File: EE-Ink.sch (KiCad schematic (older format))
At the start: 24 parts, among them U1 ED060SC4

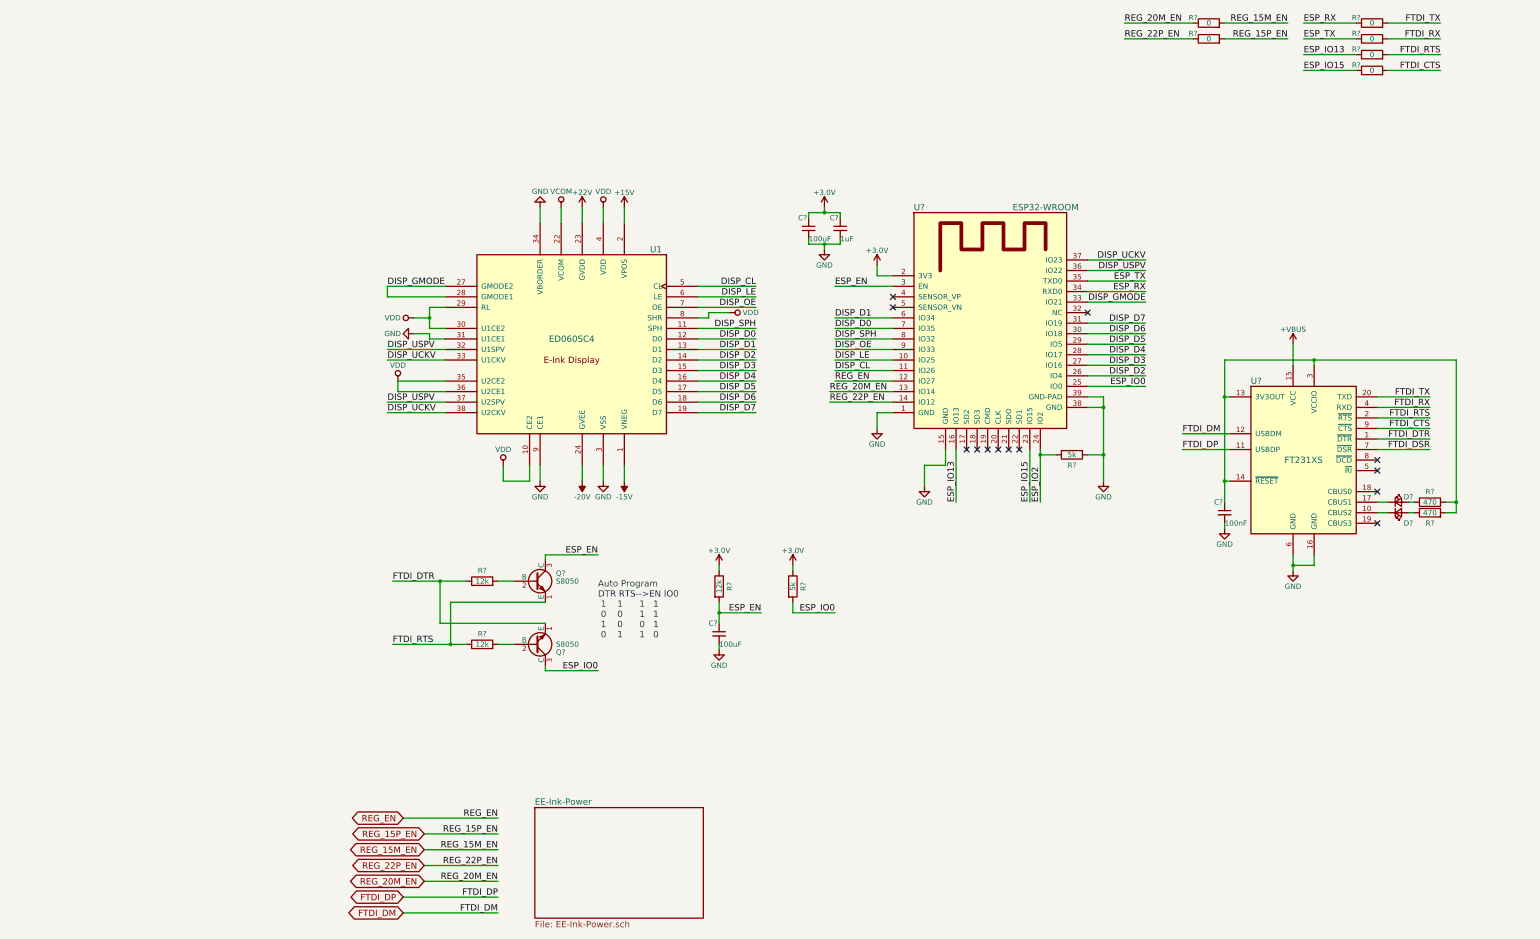
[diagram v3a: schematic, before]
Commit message: Switched out the regulator for a 500ma one.  Cleaned up a few things.
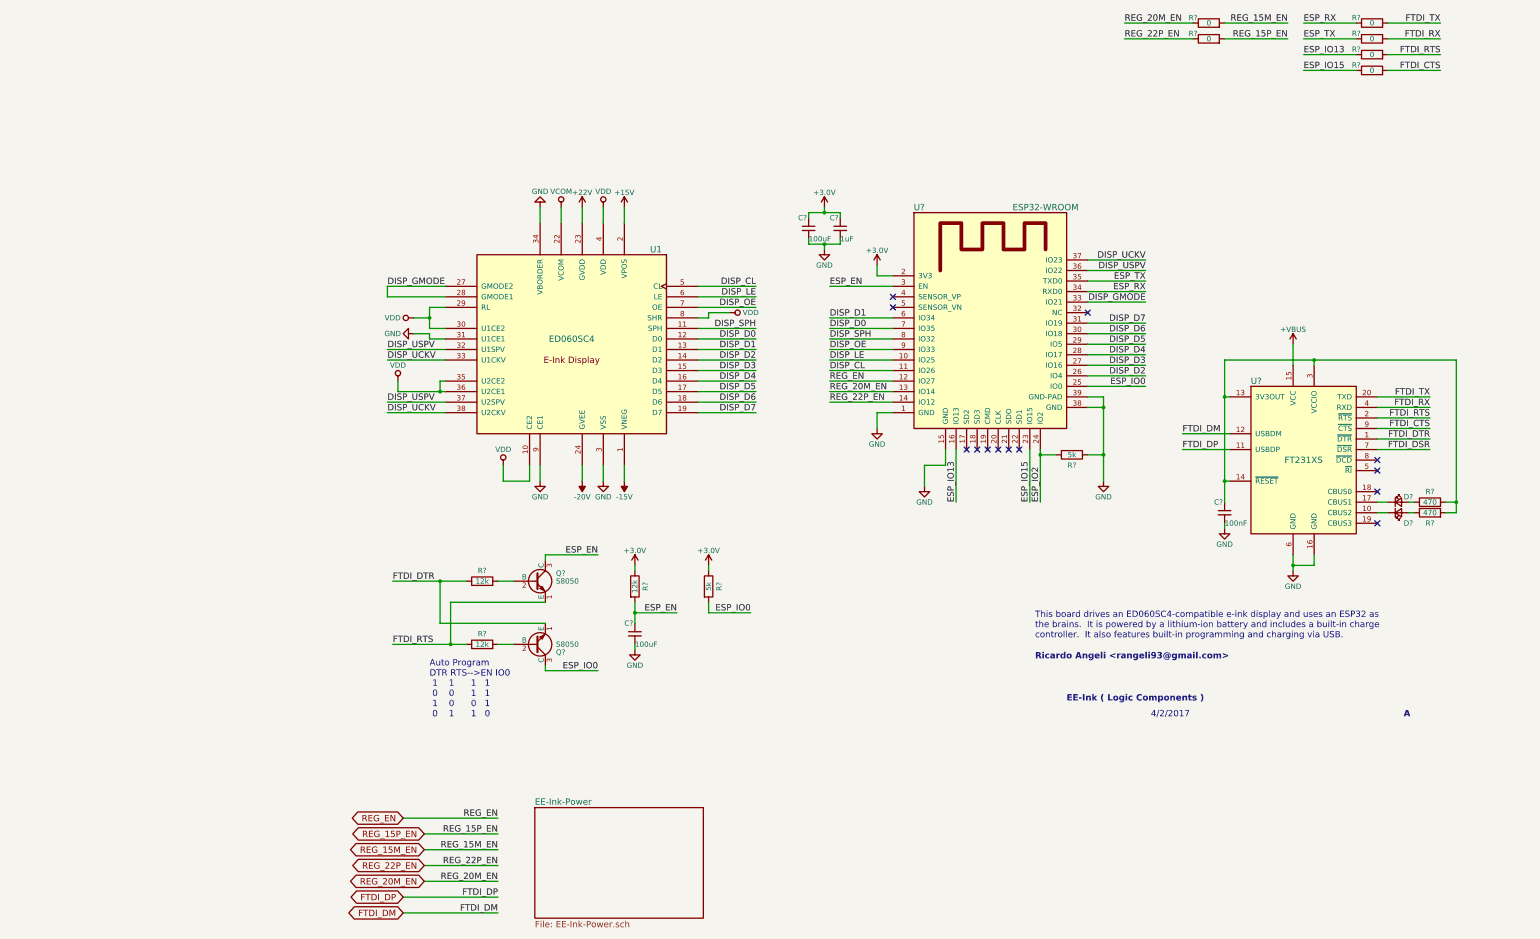
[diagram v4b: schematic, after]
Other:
- note added: "4/2/2017"
- note added: "A"
- note added: "EE-Ink ( Logic Components )"
- note added: "Ricardo Angeli <rangeli93@gmail.com>"
- note added: "This board drives an ED060SC4-compatible e-ink display and uses an ESP32 as\nthe brains. It is powered by a lithium-ion battery and includes a built-in charge\ncontroller. It also features built-in programming and charging via USB."
- moved on the sheet: C?, R?
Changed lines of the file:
@@
 Text Label 8100 4400 2    60   ~ 0
 DISP_D2
-Text Label 5150 3850 0    60   ~ 0
+Text Label 5100 3850 0    60   ~ 0
 DISP_D1
-Text Label 5150 3950 0    60   ~ 0
+Text Label 5100 3950 0    60   ~ 0
 DISP_D0
-Text Label 5150 4050 0    60   ~ 0
+Text Label 5100 4050 0    60   ~ 0
 DISP_SPH
-Text Label 5150 4150 0    60   ~ 0
+Text Label 5100 4150 0    60   ~ 0
 DISP_OE
-Text Label 5150 4250 0    60   ~ 0
+Text Label 5100 4250 0    60   ~ 0
 DISP_LE
-Text Label 5150 4350 0    60   ~ 0
+Text Label 5100 4350 0    60   ~ 0
 DISP_CL
 Wire Wire Line
@@
 Wire Wire Line
 	1000 4550 1000 4450
-Wire Wire Line
-	1000 4450 1450 4450
 Wire Wire Line
 	1450 3750 1300 3750
@@
 	7550 4400 8100 4400
 Wire Wire Line
-	5700 3850 5150 3850
-Wire Wire Line
-	5700 3950 5150 3950
-Wire Wire Line
-	5700 4050 5150 4050
-Wire Wire Line
-	5150 4150 5700 4150
-Wire Wire Line
-	5700 4250 5150 4250
-Wire Wire Line
-	5700 4350 5150 4350
+	5100 3850 5700 3850
+Wire Wire Line
+	5100 3950 5700 3950
+Wire Wire Line
+	5100 4050 5700 4050
+Wire Wire Line
+	5100 4150 5700 4150
+Wire Wire Line
+	5100 4250 5700 4250
+Wire Wire Line
+	5100 4350 5700 4350
 Wire Wire Line
 	900  3550 900  3650
 Wire Wire Line
-	5700 4450 5150 4450
-Text Label 5150 4450 0    60   ~ 0
+	5100 4450 5700 4450
+Text Label 5100 4450 0    60   ~ 0
 REG_EN
 Text Label 7900 1050 0    60   ~ 0
@@
 Text Label 9600 1050 0    60   ~ 0
 ESP_RX
-Text Notes 2900 6900 0    60   ~ 0
+Text Notes 1300 7650 0    60   ~ 0
    Auto Program\nDTR RTS-->EN IO0\n 1    1      1   1\n 0    0      1   1\n 1    0      0   1\n 0    1      1   0
 $Comp
@@
 	1    0    0    -1
 $EndComp
-Text Label 5150 3550 0    60   ~ 0
+Text Label 5100 3550 0    60   ~ 0
 ESP_EN
 Wire Wire Line
-	5700 3550 5150 3550
+	5100 3550 5700 3550
 $Comp
 L GND #PWR?
@@
 L R R?
 U 1 1 58E22CAC
-P 4050 6400
-F 0 "R?" V 4150 6400 50  0000 C CNN
-F 1 "12k" V 4050 6400 50  0000 C CNN
-F 2 "" V 3980 6400 50  0001 C CNN
-F 3 "" H 4050 6400 50  0001 C CNN
-	1    4050 6400
+P 3250 6400
+F 0 "R?" V 3350 6400 50  0000 C CNN
+F 1 "12k" V 3250 6400 50  0000 C CNN
+F 2 "" V 3180 6400 50  0001 C CNN
+F 3 "" H 3250 6400 50  0001 C CNN
+	1    3250 6400
 	1    0    0    -1
 $EndComp
@@
 L C_Small C?
 U 1 1 58E22FC2
-P 4050 6850
-F 0 "C?" H 3950 6950 50  0000 L CNN
-F 1 "100uF" H 4050 6750 50  0000 L CNN
-F 2 "" H 4050 6850 50  0001 C CNN
-F 3 "" H 4050 6850 50  0001 C CNN
-	1    4050 6850
-	1    0    0    -1
-$EndComp
-Text Label 4450 6650 2    60   ~ 0
+P 3250 6850
+F 0 "C?" H 3150 6950 50  0000 L CNN
+F 1 "100uF" H 3250 6750 50  0000 L CNN
+F 2 "" H 3250 6850 50  0001 C CNN
+F 3 "" H 3250 6850 50  0001 C CNN
+	1    3250 6850
+	1    0    0    -1
+$EndComp
+Text Label 3650 6650 2    60   ~ 0
 ESP_EN
 Wire Wire Line
-	4450 6650 4050 6650
-Wire Wire Line
-	4050 6550 4050 6750
-Connection ~ 4050 6650
+	3650 6650 3250 6650
+Wire Wire Line
+	3250 6550 3250 6750
+Connection ~ 3250 6650
 $Comp
 L +3.0V #PWR?
 U 1 1 58E23716
-P 4050 6200
-F 0 "#PWR?" H 4050 6050 50  0001 C CNN
-F 1 "+3.0V" H 4050 6340 50  0000 C CNN
-F 2 "" H 4050 6200 50  0001 C CNN
-F 3 "" H 4050 6200 50  0001 C CNN
-	1    4050 6200
-	1    0    0    -1
-$EndComp
-Wire Wire Line
-	4050 6200 4050 6250
+P 3250 6200
+F 0 "#PWR?" H 3250 6050 50  0001 C CNN
+F 1 "+3.0V" H 3250 6340 50  0000 C CNN
+F 2 "" H 3250 6200 50  0001 C CNN
+F 3 "" H 3250 6200 50  0001 C CNN
+	1    3250 6200
+	1    0    0    -1
+$EndComp
+Wire Wire Line
+	3250 6200 3250 6250
 $Comp
 L GND #PWR?
 U 1 1 58E2382F
-P 4050 7000
-F 0 "#PWR?" H 4050 6750 50  0001 C CNN
-F 1 "GND" H 4050 6850 50  0000 C CNN
-F 2 "" H 4050 7000 50  0001 C CNN
-F 3 "" H 4050 7000 50  0001 C CNN
-	1    4050 7000
-	1    0    0    -1
-$EndComp
-Wire Wire Line
-	4050 7000 4050 6950
+P 3250 7000
+F 0 "#PWR?" H 3250 6750 50  0001 C CNN
+F 1 "GND" H 3250 6850 50  0000 C CNN
+F 2 "" H 3250 7000 50  0001 C CNN
+F 3 "" H 3250 7000 50  0001 C CNN
+	1    3250 7000
+	1    0    0    -1
+$EndComp
+Wire Wire Line
+	3250 7000 3250 6950
 Text Label 8100 3500 2    60   ~ 0
 ESP_TX
@@
 L R R?
 U 1 1 58E27988
-P 4750 6400
-F 0 "R?" V 4850 6400 50  0000 C CNN
-F 1 "5k" V 4750 6400 50  0000 C CNN
-F 2 "" V 4680 6400 50  0001 C CNN
-F 3 "" H 4750 6400 50  0001 C CNN
-	1    4750 6400
-	1    0    0    -1
-$EndComp
-Text Label 5150 6650 2    60   ~ 0
+P 3950 6400
+F 0 "R?" V 4050 6400 50  0000 C CNN
+F 1 "5k" V 3950 6400 50  0000 C CNN
+F 2 "" V 3880 6400 50  0001 C CNN
+F 3 "" H 3950 6400 50  0001 C CNN
+	1    3950 6400
+	1    0    0    -1
+$EndComp
+Text Label 4350 6650 2    60   ~ 0
 ESP_IO0
 $Comp
 L +3.0V #PWR?
 U 1 1 58E27992
-P 4750 6200
-F 0 "#PWR?" H 4750 6050 50  0001 C CNN
-F 1 "+3.0V" H 4750 6340 50  0000 C CNN
-F 2 "" H 4750 6200 50  0001 C CNN
-F 3 "" H 4750 6200 50  0001 C CNN
-	1    4750 6200
-	1    0    0    -1
-$EndComp
-Wire Wire Line
-	4750 6200 4750 6250
-Wire Wire Line
-	4750 6550 4750 6650
-Wire Wire Line
-	4750 6650 5150 6650
+P 3950 6200
+F 0 "#PWR?" H 3950 6050 50  0001 C CNN
+F 1 "+3.0V" H 3950 6340 50  0000 C CNN
+F 2 "" H 3950 6200 50  0001 C CNN
+F 3 "" H 3950 6200 50  0001 C CNN
+	1    3950 6200
+	1    0    0    -1
+$EndComp
+Wire Wire Line
+	3950 6200 3950 6250
+Wire Wire Line
+	3950 6550 3950 6650
+Wire Wire Line
+	3950 6650 4350 6650
 Text Label 8100 4500 2    60   ~ 0
 ESP_IO0
@@
 	7550 5150 7700 5150
 Connection ~ 7700 5150
+Wire Wire Line
+	1450 4450 1400 4450
+Wire Wire Line
+	1400 4450 1400 4550
+Connection ~ 1400 4550
+Text Notes 7350 7500 0    60   ~ 12
+EE-Ink ( Logic Components )
+Text Notes 8150 7650 0    60   ~ 0
+4/2/2017
+Text Notes 7050 6900 0    60   ~ 0
+This board drives an ED060SC4-compatible e-ink display and uses an ESP32 as\nthe brains.  It is powered by a lithium-ion battery and includes a built-in charge\ncontroller.  It also features built-in programming and charging via USB.
+Text Notes 7050 7100 0    60   ~ 12
+Ricardo Angeli <rangeli93@gmail.com>
+Text Notes 10550 7650 0    60   ~ 12
+A
 $EndSCHEMATC

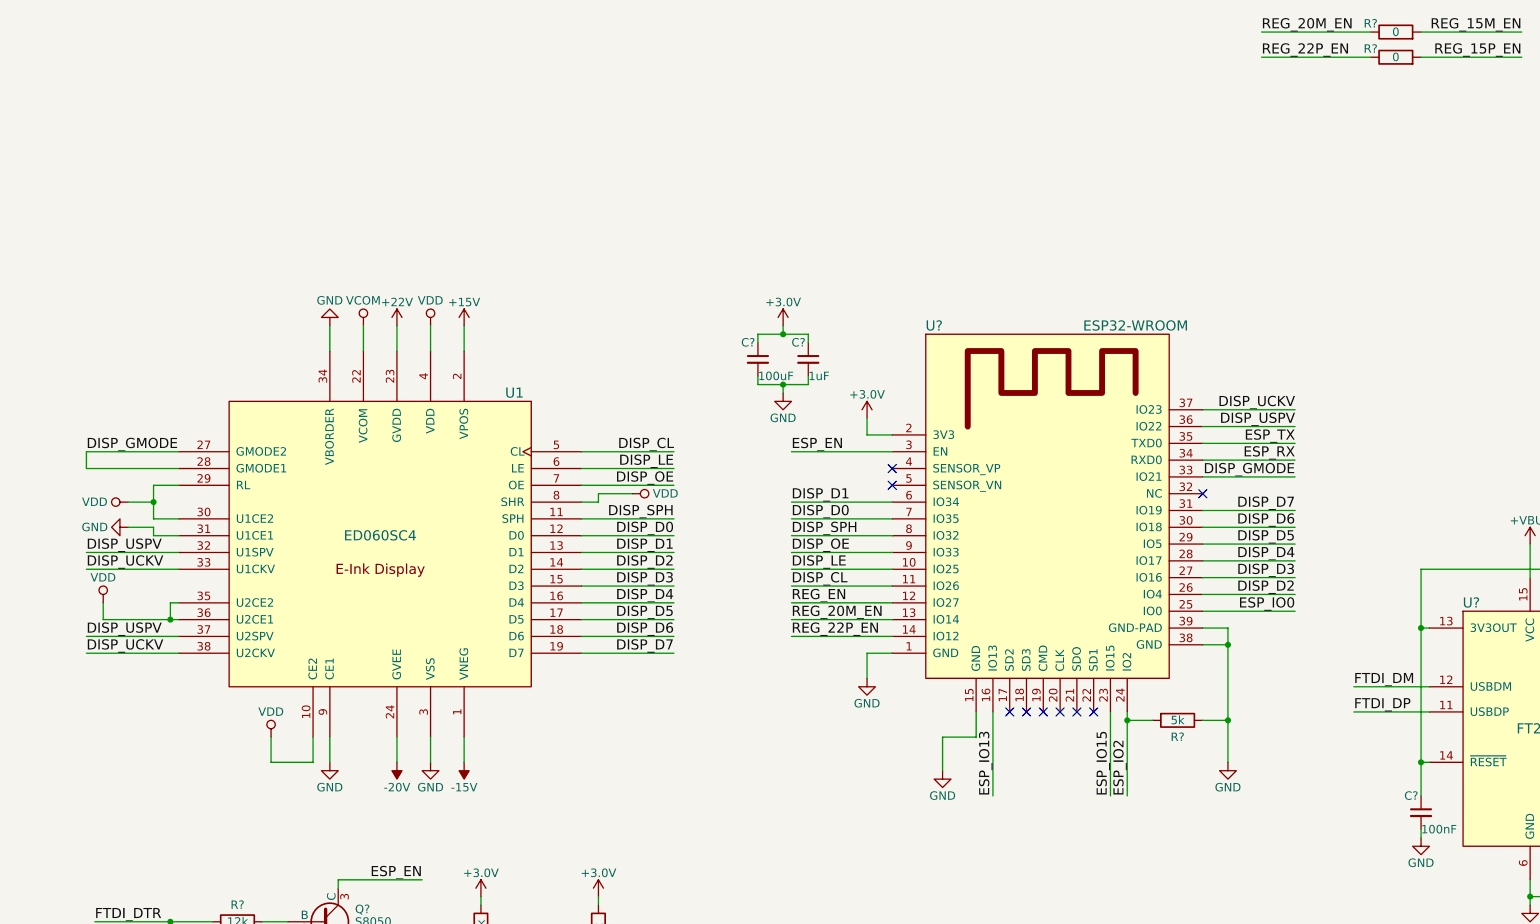
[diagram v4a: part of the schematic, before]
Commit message: Changed ESP I/O pin assignments to now use a shift register for the display's data lines.  This was caused by a couple pins found to be input only.
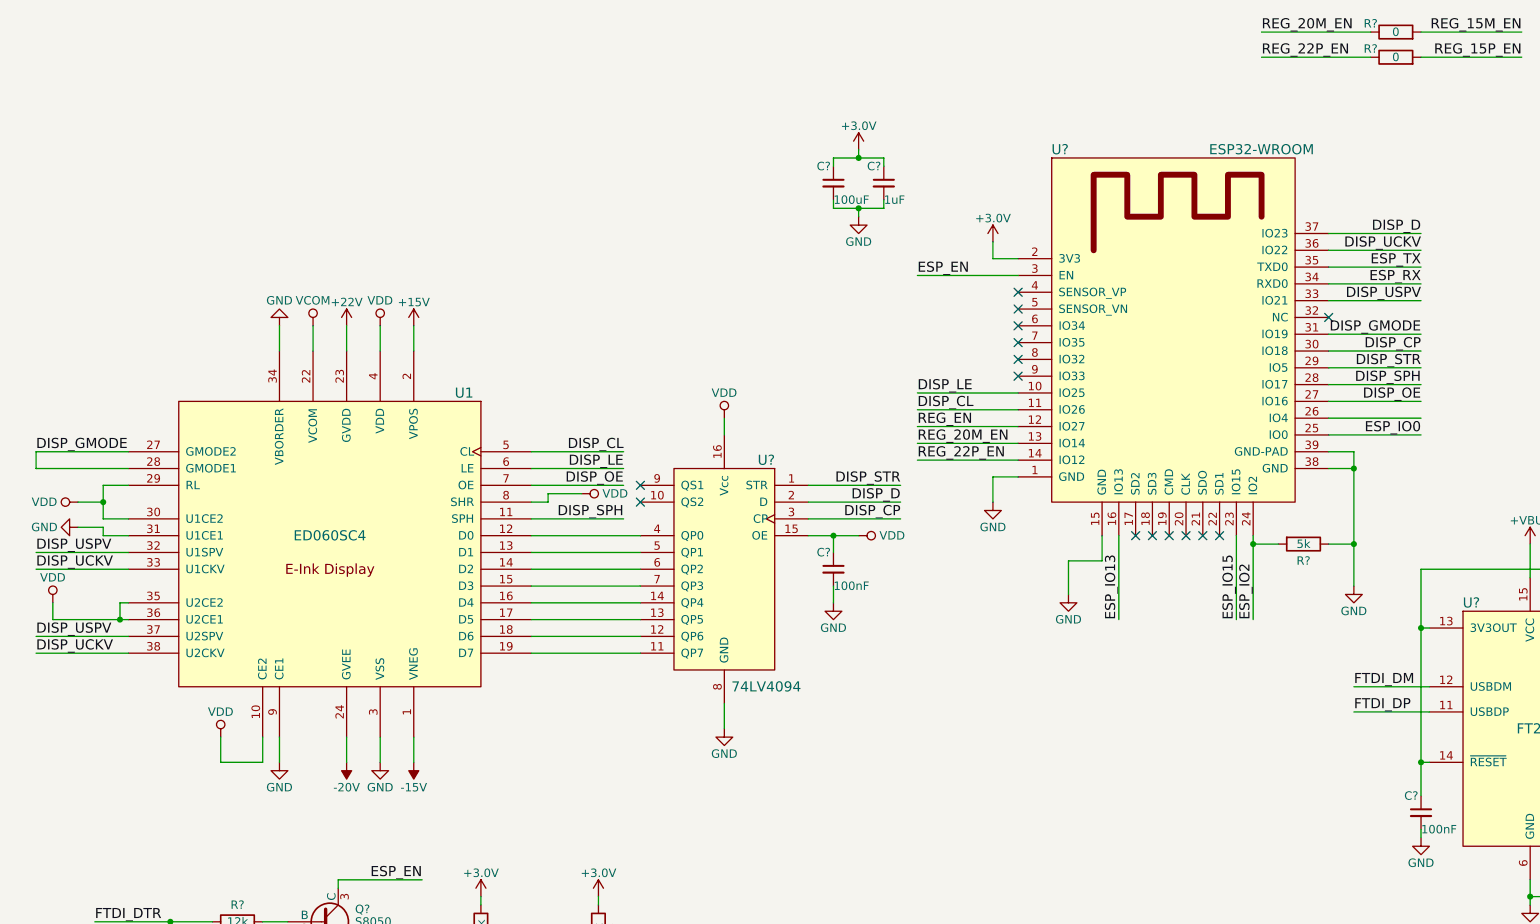
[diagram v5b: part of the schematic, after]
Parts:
- added C?: 100nF, symbol C_Small
- added U?: 74LV4094, symbol 74LV4094
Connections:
- net DISP_GMODE: now also U?.31 (IO19); no longer U?.33 (IO21)
- net DISP_OE: now also U?.27 (IO16); no longer U?.9 (IO33)
- net DISP_SPH: now also U?.28 (IO17); no longer U?.8 (IO32)
- net DISP_UCKV: now also U?.36 (IO22); no longer U?.37 (IO23)
- net DISP_USPV: now also U?.33 (IO21); no longer U?.36 (IO22)
- net GND: now also C?.2, U?.8 (GND)
- net VDD: now also C?.1, U?.15 (OE), U?.16 (Vcc)
- net DISP_D0: no longer names the net of U1.12 (D0)
- net DISP_D0: now also U?.4 (QP0); no longer U?.7 (IO35)
- net DISP_D1: no longer names the net of U1.13 (D1)
- net DISP_D1: now also U?.5 (QP1); no longer U?.6 (IO34)
- net DISP_D2: no longer names the net of U1.14 (D2)
- net DISP_D2: now also U?.6 (QP2); no longer U?.26 (IO4)
- net DISP_D3: no longer names the net of U1.15 (D3)
- net DISP_D3: now also U?.7 (QP3); no longer U?.27 (IO16)
- net DISP_D4: no longer names the net of U1.16 (D4)
- net DISP_D4: now also U?.14 (QP4); no longer U?.28 (IO17)
- net DISP_D5: no longer names the net of U1.17 (D5)
- net DISP_D5: now also U?.13 (QP5); no longer U?.29 (IO5)
- net DISP_D6: no longer names the net of U1.18 (D6)
- net DISP_D6: now also U?.12 (QP6); no longer U?.30 (IO18)
- net DISP_D7: no longer names the net of U1.19 (D7)
- net DISP_D7: now also U?.11 (QP7); no longer U?.31 (IO19)
- new net DISP_CP: U?.3 (CP), U?.30 (IO18)
- new net DISP_D: U?.2 (D), U?.37 (IO23)
- new net DISP_STR: U?.1 (STR), U?.29 (IO5)
- no-connect marks 13 -> 19
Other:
- moved on the sheet: C?, R?, U1, U?
